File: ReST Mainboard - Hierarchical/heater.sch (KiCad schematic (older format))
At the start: 40 parts, among them P27 CONN_02X06, P29 CONN_01X02, P30 CONN_01X02, P31 CONN_01X02, Q10 Q_AOT240L, Q11 Q_AOT240L, Q12 Q_AOT240L, Q7 Q_BSH105/IRLML2502, Q8 Q_BSH105/IRLML2502, Q9 Q_BSH105/IRLML2502

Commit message: started routing
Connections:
- net TEMP_0: now also C37.1; no longer C36.1
- net TEMP_1: now also C36.1; no longer C37.1
- net H2_GATE: now reaches Q10.1 (G), R41.2
- net H2_GATE: now also Q12.1 (G), R43.2
- net H1_GATE: now reaches Q11.1 (G), R42.2
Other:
- moved on the sheet: C36, C37
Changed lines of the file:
@@
 L C_Small C36
 U 1 1 577304AB
-P 7850 2400
-F 0 "C36" H 7860 2470 50  0000 L CNN
-F 1 "10uF" H 7860 2320 50  0000 L CNN
-F 2 "Capacitors_SMD:C_0805_HandSoldering" H 7850 2400 50  0001 C CNN
-F 3 "" H 7850 2400 50  0000 C CNN
-	1    7850 2400
+P 8550 2400
+F 0 "C36" H 8560 2470 50  0000 L CNN
+F 1 "10uF" H 8560 2320 50  0000 L CNN
+F 2 "Capacitors_SMD:C_0805_HandSoldering" H 8550 2400 50  0001 C CNN
+F 3 "" H 8550 2400 50  0000 C CNN
+	1    8550 2400
 	1    0    0    -1
 $EndComp
@@
 L C_Small C37
 U 1 1 57734137
-P 8550 2400
-F 0 "C37" H 8560 2470 50  0000 L CNN
-F 1 "10uF" H 8560 2320 50  0000 L CNN
-F 2 "Capacitors_SMD:C_0805_HandSoldering" H 8550 2400 50  0001 C CNN
-F 3 "" H 8550 2400 50  0000 C CNN
-	1    8550 2400
+P 7850 2400
+F 0 "C37" H 7860 2470 50  0000 L CNN
+F 1 "10uF" H 7860 2320 50  0000 L CNN
+F 2 "Capacitors_SMD:C_0805_HandSoldering" H 7850 2400 50  0001 C CNN
+F 3 "" H 7850 2400 50  0000 C CNN
+	1    7850 2400
 	1    0    0    -1
 $EndComp
@@
 	1    0    0    -1
 $EndComp
+Text Label 3850 2250 1    39   ~ 0
+H2_GATE
+Text Label 3850 3600 1    39   ~ 0
+H1_GATE
+Text Label 3850 4950 1    39   ~ 0
+H2_GATE
 $EndSCHEMATC

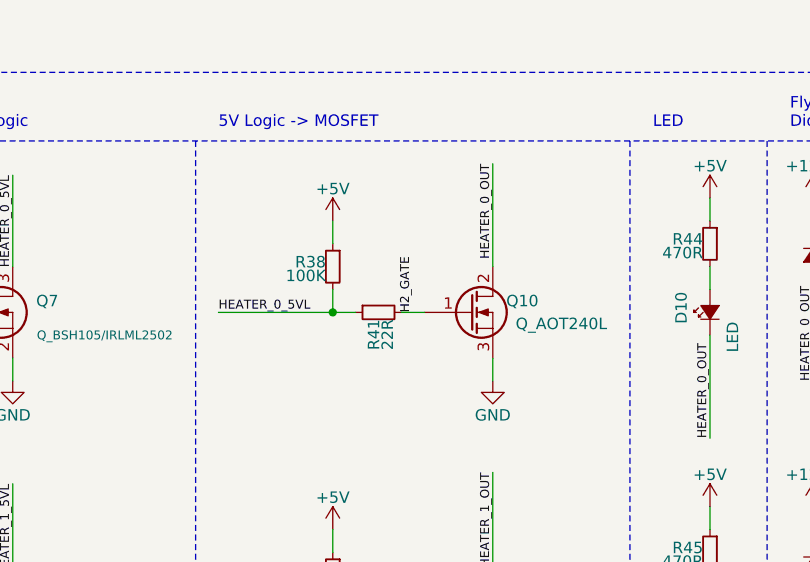
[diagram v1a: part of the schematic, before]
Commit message: electrically finished. in the works of the silkscreening.
Schematic for SD Card Adapter and a RepRapDiscount-Adapter in the works. but not in this commit
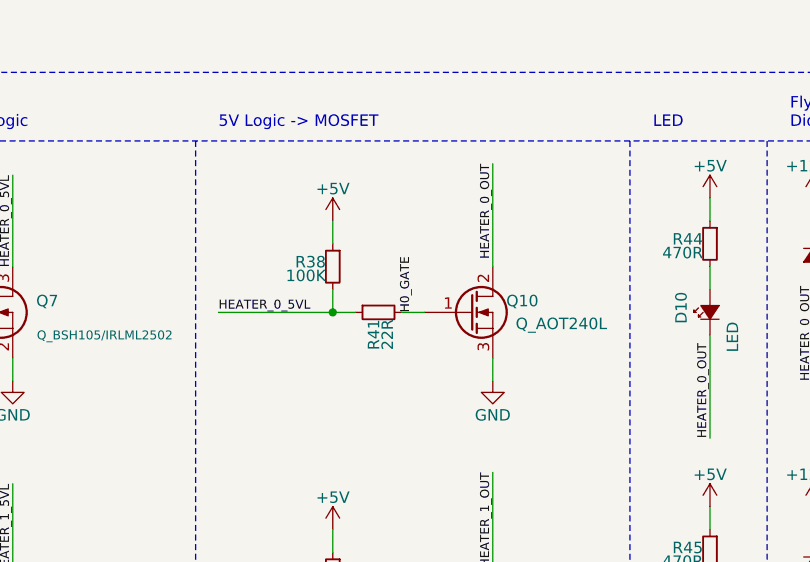
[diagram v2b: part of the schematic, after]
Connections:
- net H2_GATE: no longer Q10.1 (G), R41.2
- new net H0_GATE: Q10.1 (G), R41.2
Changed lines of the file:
@@
 	9800 1550 9800 4150
-Wire Notes Line
-	7700 1550 7700 4150
 Wire Notes Line
 	8400 1550 8400 4150
@@
 $EndComp
 Text Label 3850 2250 1    39   ~ 0
-H2_GATE
+H0_GATE
 Text Label 3850 3600 1    39   ~ 0
 H1_GATE
 Text Label 3850 4950 1    39   ~ 0
 H2_GATE
+Wire Notes Line
+	7700 1550 7700 4150
 $EndSCHEMATC

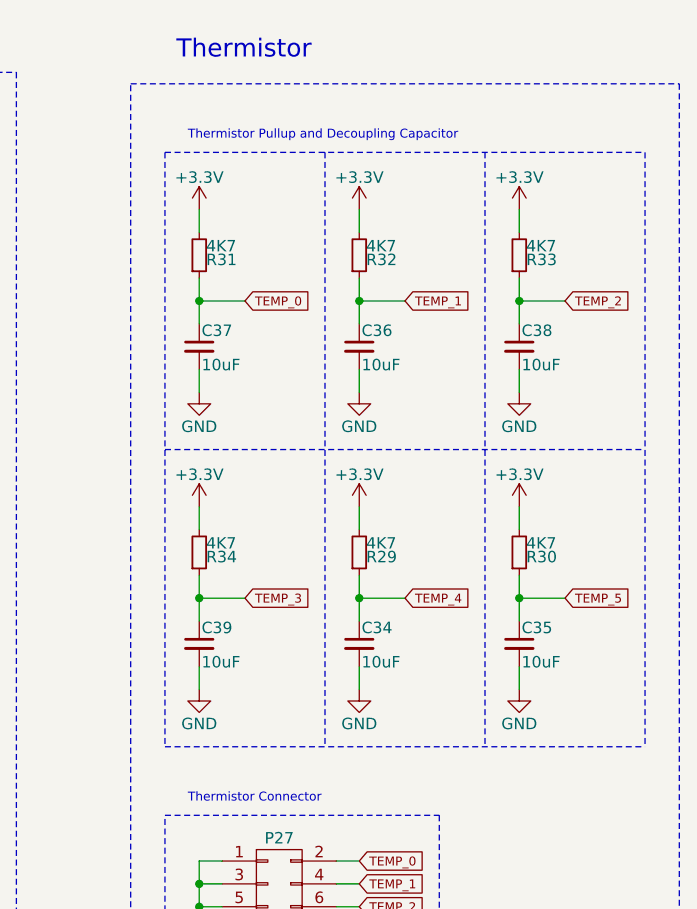
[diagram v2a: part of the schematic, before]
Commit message: added ESP-01 Support
Afterthought, completely forgot about it
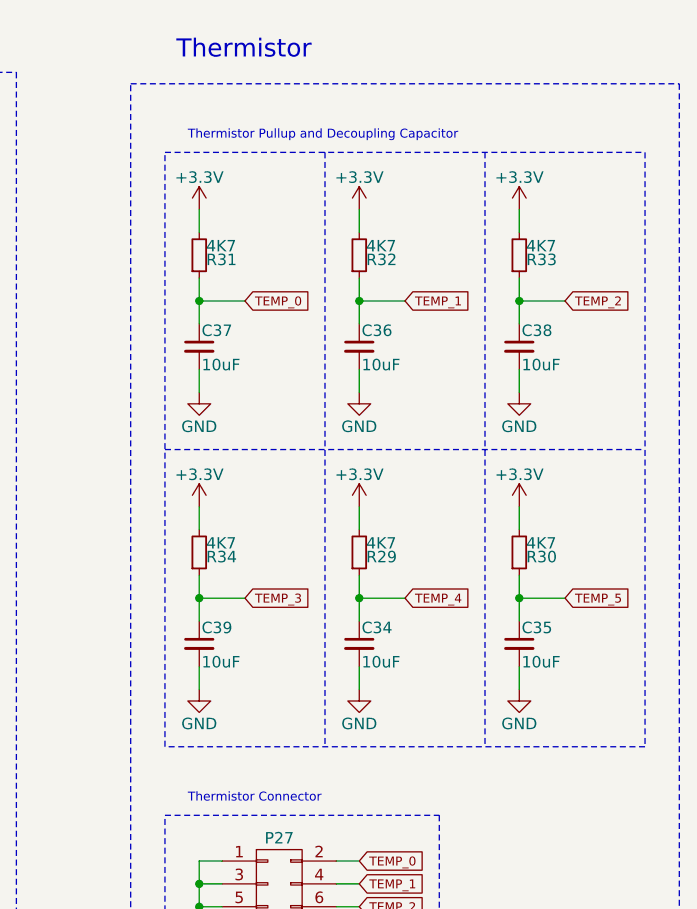
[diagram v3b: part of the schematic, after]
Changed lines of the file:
@@
 $EndComp
 $Comp
-L GND #PWR01
+L GND #PWR26
 U 1 1 5773047F
 P 7850 5250
-F 0 "#PWR01" H 7850 5000 50  0001 C CNN
+F 0 "#PWR26" H 7850 5000 50  0001 C CNN
 F 1 "GND" H 7850 5100 50  0000 C CNN
 F 2 "" H 7850 5250 50  0000 C CNN
@@
 $EndComp
 $Comp
-L +3.3V #PWR02
+L +3.3V #PWR22
 U 1 1 577304A5
 P 7850 1800
-F 0 "#PWR02" H 7850 1650 50  0001 C CNN
+F 0 "#PWR22" H 7850 1650 50  0001 C CNN
 F 1 "+3.3V" H 7850 1940 50  0000 C CNN
 F 2 "" H 7850 1800 50  0000 C CNN
@@
 $EndComp
 $Comp
-L GND #PWR03
+L GND #PWR23
 U 1 1 577304B2
 P 7850 2600
-F 0 "#PWR03" H 7850 2350 50  0001 C CNN
+F 0 "#PWR23" H 7850 2350 50  0001 C CNN
 F 1 "GND" H 7850 2450 50  0000 C CNN
 F 2 "" H 7850 2600 50  0000 C CNN
@@
 $EndComp
 $Comp
-L +3.3V #PWR04
+L +3.3V #PWR27
 U 1 1 57734131
 P 8550 1800
-F 0 "#PWR04" H 8550 1650 50  0001 C CNN
+F 0 "#PWR27" H 8550 1650 50  0001 C CNN
 F 1 "+3.3V" H 8550 1940 50  0000 C CNN
 F 2 "" H 8550 1800 50  0000 C CNN
@@
 $EndComp
 $Comp
-L GND #PWR05
+L GND #PWR28
 U 1 1 5773413D
 P 8550 2600
-F 0 "#PWR05" H 8550 2350 50  0001 C CNN
+F 0 "#PWR28" H 8550 2350 50  0001 C CNN
 F 1 "GND" H 8550 2450 50  0000 C CNN
 F 2 "" H 8550 2600 50  0000 C CNN
@@
 $EndComp
 $Comp
-L +3.3V #PWR06
+L +3.3V #PWR31
 U 1 1 5773421C
 P 9250 1800
-F 0 "#PWR06" H 9250 1650 50  0001 C CNN
+F 0 "#PWR31" H 9250 1650 50  0001 C CNN
 F 1 "+3.3V" H 9250 1940 50  0000 C CNN
 F 2 "" H 9250 1800 50  0000 C CNN
@@
 $EndComp
 $Comp
-L GND #PWR07
+L GND #PWR32
 U 1 1 57734229
 P 9250 2600
-F 0 "#PWR07" H 9250 2350 50  0001 C CNN
+F 0 "#PWR32" H 9250 2350 50  0001 C CNN
 F 1 "GND" H 9250 2450 50  0000 C CNN
 F 2 "" H 9250 2600 50  0000 C CNN
@@
 $EndComp
 $Comp
-L +3.3V #PWR08
+L +3.3V #PWR24
 U 1 1 57734300
 P 7850 3100
-F 0 "#PWR08" H 7850 2950 50  0001 C CNN
+F 0 "#PWR24" H 7850 2950 50  0001 C CNN
 F 1 "+3.3V" H 7850 3240 50  0000 C CNN
 F 2 "" H 7850 3100 50  0000 C CNN
@@
 $EndComp
 $Comp
-L GND #PWR09
+L GND #PWR25
 U 1 1 5773430D
 P 7850 3900
-F 0 "#PWR09" H 7850 3650 50  0001 C CNN
+F 0 "#PWR25" H 7850 3650 50  0001 C CNN
 F 1 "GND" H 7850 3750 50  0000 C CNN
 F 2 "" H 7850 3900 50  0000 C CNN
@@
 $EndComp
 $Comp
-L +3.3V #PWR010
+L +3.3V #PWR29
 U 1 1 5773445C
 P 8550 3100
-F 0 "#PWR010" H 8550 2950 50  0001 C CNN
+F 0 "#PWR29" H 8550 2950 50  0001 C CNN
 F 1 "+3.3V" H 8550 3240 50  0000 C CNN
 F 2 "" H 8550 3100 50  0000 C CNN
@@
 $EndComp
 $Comp
-L GND #PWR011
+L GND #PWR30
 U 1 1 57734469
 P 8550 3900
-F 0 "#PWR011" H 8550 3650 50  0001 C CNN
+F 0 "#PWR30" H 8550 3650 50  0001 C CNN
 F 1 "GND" H 8550 3750 50  0000 C CNN
 F 2 "" H 8550 3900 50  0000 C CNN
@@
 $EndComp
 $Comp
-L +3.3V #PWR012
+L +3.3V #PWR33
 U 1 1 577344EF
 P 9250 3100
-F 0 "#PWR012" H 9250 2950 50  0001 C CNN
+F 0 "#PWR33" H 9250 2950 50  0001 C CNN
 F 1 "+3.3V" H 9250 3240 50  0000 C CNN
 F 2 "" H 9250 3100 50  0000 C CNN
@@
 $EndComp
 $Comp
-L GND #PWR013
+L GND #PWR34
 U 1 1 577344FC
 P 9250 3900
-F 0 "#PWR013" H 9250 3650 50  0001 C CNN
+F 0 "#PWR34" H 9250 3650 50  0001 C CNN
 F 1 "GND" H 9250 3750 50  0000 C CNN
 F 2 "" H 9250 3900 50  0000 C CNN
@@
 HEATER_0
 $Comp
-L +5V #PWR014
+L +5V #PWR7
 U 1 1 57744A96
 P 3500 1850
-F 0 "#PWR014" H 3500 1700 50  0001 C CNN
+F 0 "#PWR7" H 3500 1700 50  0001 C CNN
 F 1 "+5V" H 3500 1990 50  0000 C CNN
 F 2 "" H 3500 1850 50  0000 C CNN
@@
 $EndComp
 $Comp
-L GND #PWR015
+L GND #PWR4
 U 1 1 57744AA2
 P 2100 2550
-F 0 "#PWR015" H 2100 2300 50  0001 C CNN
+F 0 "#PWR4" H 2100 2300 50  0001 C CNN
 F 1 "GND" H 2100 2400 50  0000 C CNN
 F 2 "" H 2100 2550 50  0000 C CNN
@@
 $EndComp
 $Comp
-L +3.3V #PWR016
+L +3.3V #PWR1
 U 1 1 57744AA8
 P 1700 1850
-F 0 "#PWR016" H 1700 1700 50  0001 C CNN
+F 0 "#PWR1" H 1700 1700 50  0001 C CNN
 F 1 "+3.3V" H 1700 1990 50  0000 C CNN
 F 2 "" H 1700 1850 50  0000 C CNN
@@
 HEATER_0_5VL
 $Comp
-L GND #PWR017
+L GND #PWR10
 U 1 1 5774B37D
 P 4200 2550
-F 0 "#PWR017" H 4200 2300 50  0001 C CNN
+F 0 "#PWR10" H 4200 2300 50  0001 C CNN
 F 1 "GND" H 4200 2400 50  0000 C CNN
 F 2 "" H 4200 2550 50  0000 C CNN
@@
 $EndComp
 $Comp
-L +5V #PWR018
+L +5V #PWR13
 U 1 1 57752FAF
 P 5150 1750
-F 0 "#PWR018" H 5150 1600 50  0001 C CNN
+F 0 "#PWR13" H 5150 1600 50  0001 C CNN
 F 1 "+5V" H 5150 1890 50  0000 C CNN
 F 2 "" H 5150 1750 50  0000 C CNN
@@
 $EndComp
 $Comp
-L +12VA #PWR019
+L +12VA #PWR19
 U 1 1 577584CF
 P 6350 1800
-F 0 "#PWR019" H 6350 1650 50  0001 C CNN
+F 0 "#PWR19" H 6350 1650 50  0001 C CNN
 F 1 "+12VA" H 6350 1940 50  0000 C CNN
 F 2 "" H 6350 1800 50  0000 C CNN
@@
 HEATER_0_OUT
 $Comp
-L +12VA #PWR020
+L +12VA #PWR16
 U 1 1 57759170
 P 5600 1750
-F 0 "#PWR020" H 5600 1600 50  0001 C CNN
+F 0 "#PWR16" H 5600 1600 50  0001 C CNN
 F 1 "+12VA" H 5600 1890 50  0000 C CNN
 F 2 "" H 5600 1750 50  0000 C CNN
@@
 HEATER_1
 $Comp
-L +5V #PWR021
+L +5V #PWR8
 U 1 1 57767992
 P 3500 3200
-F 0 "#PWR021" H 3500 3050 50  0001 C CNN
+F 0 "#PWR8" H 3500 3050 50  0001 C CNN
 F 1 "+5V" H 3500 3340 50  0000 C CNN
 F 2 "" H 3500 3200 50  0000 C CNN
@@
 $EndComp
 $Comp
-L GND #PWR022
+L GND #PWR5
 U 1 1 57767998
 P 2100 3900
-F 0 "#PWR022" H 2100 3650 50  0001 C CNN
+F 0 "#PWR5" H 2100 3650 50  0001 C CNN
 F 1 "GND" H 2100 3750 50  0000 C CNN
 F 2 "" H 2100 3900 50  0000 C CNN
@@
 $EndComp
 $Comp
-L +3.3V #PWR023
+L +3.3V #PWR2
 U 1 1 5776799E
 P 1700 3200
-F 0 "#PWR023" H 1700 3050 50  0001 C CNN
+F 0 "#PWR2" H 1700 3050 50  0001 C CNN
 F 1 "+3.3V" H 1700 3340 50  0000 C CNN
 F 2 "" H 1700 3200 50  0000 C CNN
@@
 HEATER_1_5VL
 $Comp
-L GND #PWR024
+L GND #PWR11
 U 1 1 577679B1
 P 4200 3900
-F 0 "#PWR024" H 4200 3650 50  0001 C CNN
+F 0 "#PWR11" H 4200 3650 50  0001 C CNN
 F 1 "GND" H 4200 3750 50  0000 C CNN
 F 2 "" H 4200 3900 50  0000 C CNN
@@
 $EndComp
 $Comp
-L +5V #PWR025
+L +5V #PWR14
 U 1 1 577679C5
 P 5150 3100
-F 0 "#PWR025" H 5150 2950 50  0001 C CNN
+F 0 "#PWR14" H 5150 2950 50  0001 C CNN
 F 1 "+5V" H 5150 3240 50  0000 C CNN
 F 2 "" H 5150 3100 50  0000 C CNN
@@
 HEATER_2
 $Comp
-L +5V #PWR026
+L +5V #PWR9
 U 1 1 57768FD0
 P 3500 4550
-F 0 "#PWR026" H 3500 4400 50  0001 C CNN
+F 0 "#PWR9" H 3500 4400 50  0001 C CNN
 F 1 "+5V" H 3500 4690 50  0000 C CNN
 F 2 "" H 3500 4550 50  0000 C CNN
@@
 $EndComp
 $Comp
-L GND #PWR027
+L GND #PWR6
 U 1 1 57768FD6
 P 2100 5250
-F 0 "#PWR027" H 2100 5000 50  0001 C CNN
+F 0 "#PWR6" H 2100 5000 50  0001 C CNN
 F 1 "GND" H 2100 5100 50  0000 C CNN
 F 2 "" H 2100 5250 50  0000 C CNN
@@
 $EndComp
 $Comp
-L +3.3V #PWR028
+L +3.3V #PWR3
 U 1 1 57768FDC
 P 1700 4550
-F 0 "#PWR028" H 1700 4400 50  0001 C CNN
+F 0 "#PWR3" H 1700 4400 50  0001 C CNN
 F 1 "+3.3V" H 1700 4690 50  0000 C CNN
 F 2 "" H 1700 4550 50  0000 C CNN
@@
 HEATER_2_5VL
 $Comp
-L GND #PWR029
+L GND #PWR12
 U 1 1 57768FEF
 P 4200 5250
-F 0 "#PWR029" H 4200 5000 50  0001 C CNN
+F 0 "#PWR12" H 4200 5000 50  0001 C CNN
 F 1 "GND" H 4200 5100 50  0000 C CNN
 F 2 "" H 4200 5250 50  0000 C CNN
@@
 $EndComp
 $Comp
-L +5V #PWR030
+L +5V #PWR15
 U 1 1 57769003
 P 5150 4450
-F 0 "#PWR030" H 5150 4300 50  0001 C CNN
+F 0 "#PWR15" H 5150 4300 50  0001 C CNN
 F 1 "+5V" H 5150 4590 50  0000 C CNN
 F 2 "" H 5150 4450 50  0000 C CNN
@@
 	7700 2850 9800 2850
 Wire Notes Line
-	7700 4150 9800 4150
+	9800 4150 7700 4150
 Wire Notes Line
 	7700 1550 9800 1550
@@
 Thermistor
 $Comp
-L +12VA #PWR031
+L +12VA #PWR17
 U 1 1 57791482
 P 5600 3100
-F 0 "#PWR031" H 5600 2950 50  0001 C CNN
+F 0 "#PWR17" H 5600 2950 50  0001 C CNN
 F 1 "+12VA" H 5600 3240 50  0000 C CNN
 F 2 "" H 5600 3100 50  0000 C CNN
@@
 $EndComp
 $Comp
-L +12VA #PWR032
+L +12VA #PWR18
 U 1 1 57791505
 P 5600 4450
-F 0 "#PWR032" H 5600 4300 50  0001 C CNN
+F 0 "#PWR18" H 5600 4300 50  0001 C CNN
 F 1 "+12VA" H 5600 4590 50  0000 C CNN
 F 2 "" H 5600 4450 50  0000 C CNN
@@
 $EndComp
 $Comp
-L +12VA #PWR033
+L +12VA #PWR21
 U 1 1 57791588
 P 6350 4500
-F 0 "#PWR033" H 6350 4350 50  0001 C CNN
+F 0 "#PWR21" H 6350 4350 50  0001 C CNN
 F 1 "+12VA" H 6350 4640 50  0000 C CNN
 F 2 "" H 6350 4500 50  0000 C CNN
@@
 $EndComp
 $Comp
-L +12VA #PWR034
+L +12VA #PWR20
 U 1 1 5779160B
 P 6350 3150
-F 0 "#PWR034" H 6350 3000 50  0001 C CNN
+F 0 "#PWR20" H 6350 3000 50  0001 C CNN
 F 1 "+12VA" H 6350 3290 50  0000 C CNN
 F 2 "" H 6350 3150 50  0000 C CNN
@@
 H2_GATE
 Wire Notes Line
-	7700 1550 7700 4150
+	7700 4150 7700 1550
 $EndSCHEMATC

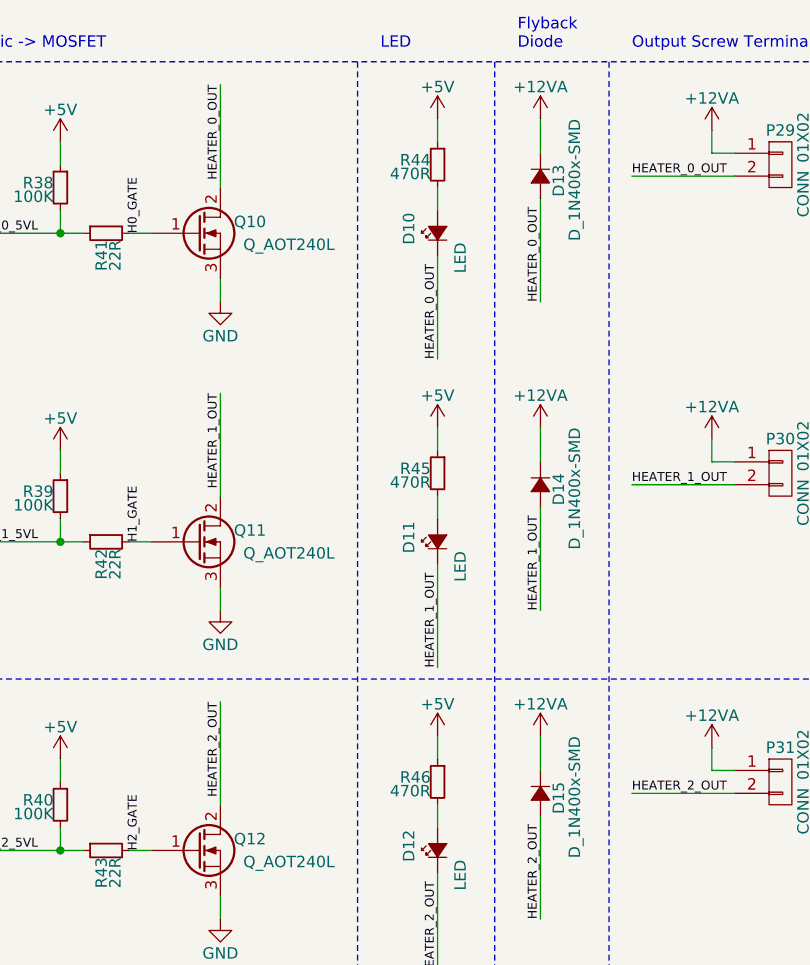
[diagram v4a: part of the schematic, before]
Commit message: minor changes to values of components and footprints. added two leds for both 12V Rails.
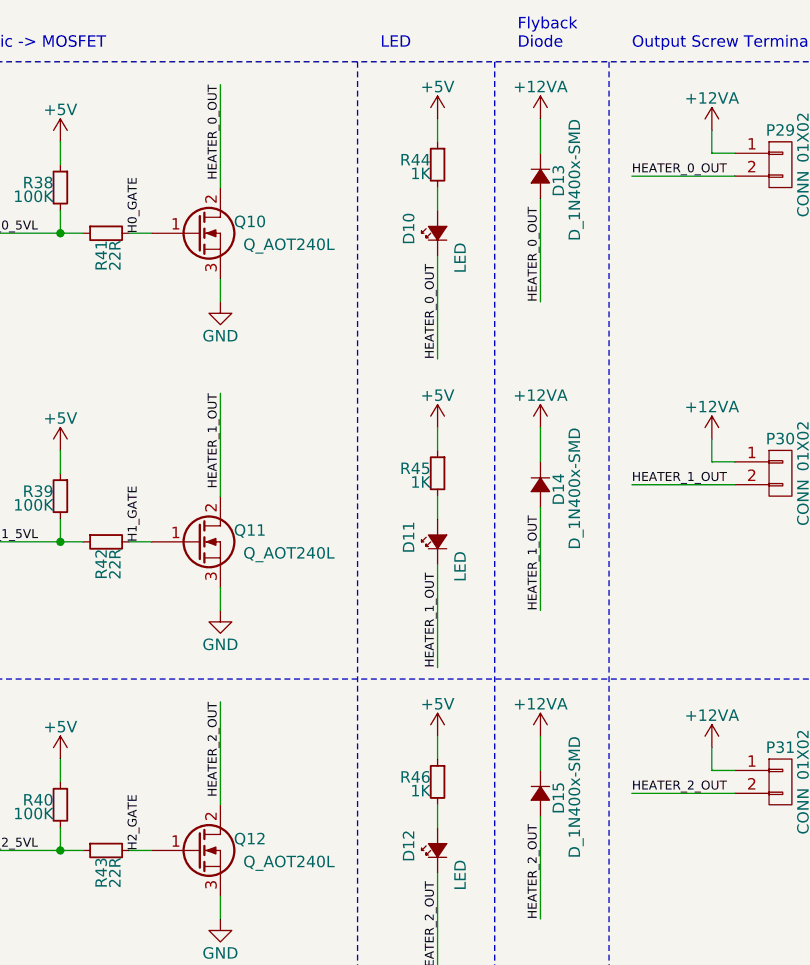
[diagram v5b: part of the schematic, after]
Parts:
- R44, R45, R46: value 470R -> 1K
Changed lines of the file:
@@
 P 5150 1950
 F 0 "R44" H 5180 1970 50  0000 L CNN
-F 1 "470R" H 5180 1910 50  0000 L CNN
+F 1 "1K" H 5180 1910 50  0000 L CNN
 F 2 "Resistors_SMD:R_0603_HandSoldering" H 5150 1950 50  0001 C CNN
 F 3 "" H 5150 1950 50  0000 C CNN
@@
 P 5150 3300
 F 0 "R45" H 5180 3320 50  0000 L CNN
-F 1 "470R" H 5180 3260 50  0000 L CNN
+F 1 "1K" H 5180 3260 50  0000 L CNN
 F 2 "Resistors_SMD:R_0603_HandSoldering" H 5150 3300 50  0001 C CNN
 F 3 "" H 5150 3300 50  0000 C CNN
@@
 P 5150 4650
 F 0 "R46" H 5180 4670 50  0000 L CNN
-F 1 "470R" H 5180 4610 50  0000 L CNN
+F 1 "1K" H 5180 4610 50  0000 L CNN
 F 2 "Resistors_SMD:R_0603_HandSoldering" H 5150 4650 50  0001 C CNN
 F 3 "" H 5150 4650 50  0000 C CNN
